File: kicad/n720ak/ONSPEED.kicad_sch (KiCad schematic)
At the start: 3 parts, among them J401 ONSPEED VOLUME POT, J402 ONSPEED BUTTON, J403 ONSPEED DB25

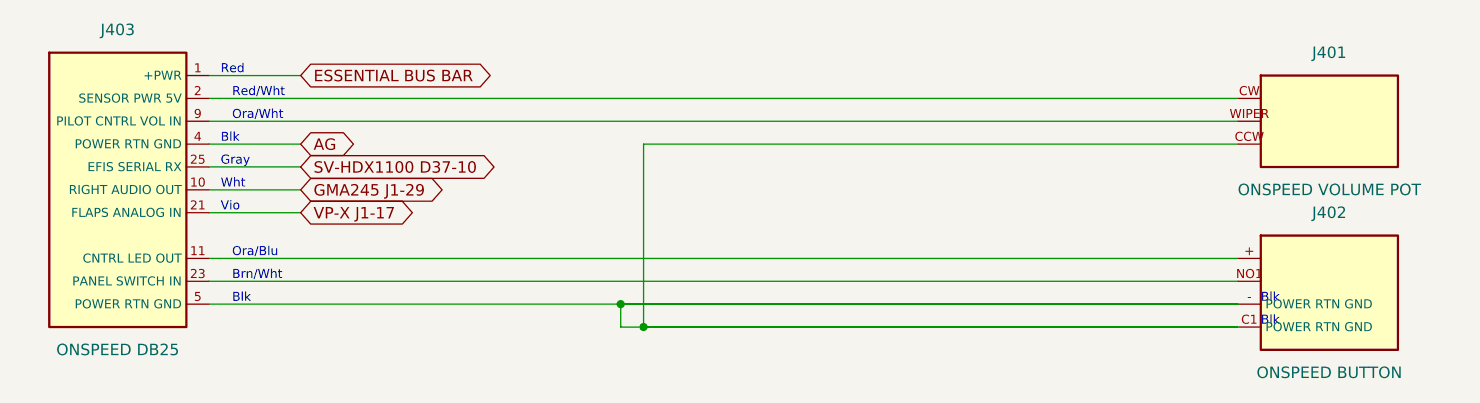
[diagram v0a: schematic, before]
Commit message: Record the third round of answers
- COM 2 flip/flop button returns to SV-COM-PANEL pin 3 (Ground out), on
  the owner's best recollection - recorded as unverified.
- OnSpeed's audio ground (pin 20) is tied to a ground pin in its own plug.
  GMA 245 Alert 3,4 Audio Lo (J1-43) is not connected, so the Alert 3
  input is single-ended.
- A panel switch disables the copilot grip trim by breaking the buttons'
  common. It is on neither SteinAir sheet, so it is recorded but flagged
  rather than drawn as a guess.
- AP disconnect is on both grips in parallel, as drawn.

Co-Authored-By: Claude Opus 5.5 <noreply@anthropic.com>
Claude-Session: https://claude.ai/code/session_015SpGdnvPFhutgEDurpngu2
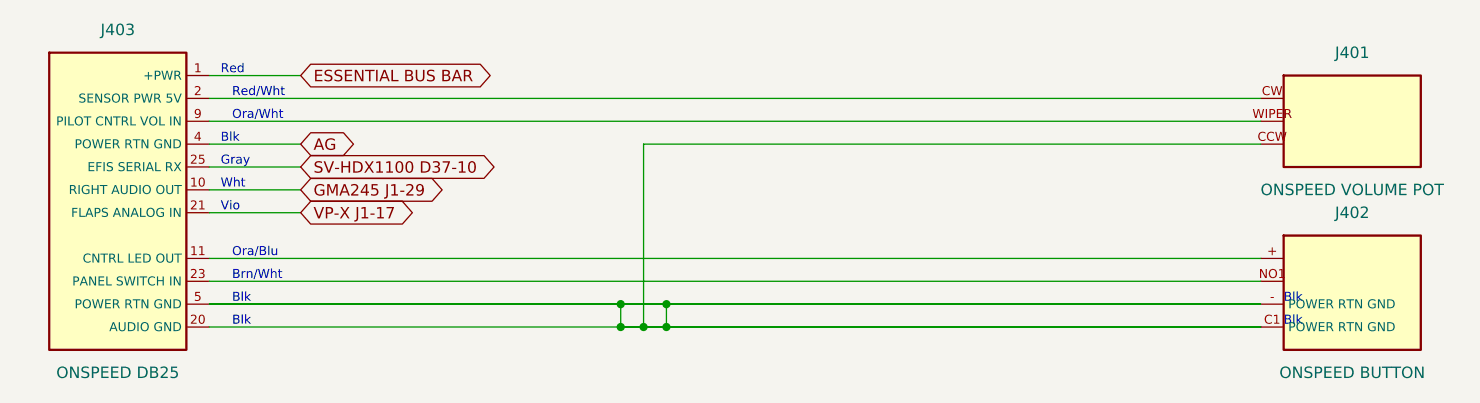
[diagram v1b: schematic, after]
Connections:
- net at J401.CCW, J402.- (POWER RTN GND), J402.C1 (POWER RTN GND)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: now also J403.20 (AUDIO GND)
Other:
- moved on the sheet: J401, J402
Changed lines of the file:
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@@
 	(paper "A3")
 	(title_block (title "OnSpeed AoA") (company "N720AK -- Van's RV-10") (comment 1 "Generated from wiring/ONSPEED.tsv -- edit the wire list, not this sheet"))
-	(symbol (lib_id "n720ak:ONSPEED_VOLUME_POT") (at 185.42 45.72 0) (unit 1)
+	(symbol (lib_id "n720ak:ONSPEED_VOLUME_POT") (at 187.96 45.72 0) (unit 1)
 		(in_bom yes) (on_board yes) (dnp no)
-		(property "Reference" "J401" (at 185.42 38.1 0) (effects (font (size 1.27 1.27))))
-		(property "Value" "ONSPEED VOLUME POT" (at 185.42 53.34 0) (effects (font (size 1.27 1.27))))
+		(property "Reference" "J401" (at 187.96 38.1 0) (effects (font (size 1.27 1.27))))
+		(property "Value" "ONSPEED VOLUME POT" (at 187.96 53.34 0) (effects (font (size 1.27 1.27))))
 		(instances (project "n720ak"
 			(path "/184b9d0a-f6b2-58e0-986b-f23064ec6643" (reference "J401") (unit 1))
 			(path "/05ae3897-9dd7-5bc2-b238-7f217081554a/2ac1f6a7-154c-57d3-8fed-8d80473941e2" (reference "J401") (unit 1)))))
-	(symbol (lib_id "n720ak:ONSPEED_BUTTON") (at 185.42 64.77 0) (unit 1)
+	(symbol (lib_id "n720ak:ONSPEED_BUTTON") (at 187.96 64.77 0) (unit 1)
 		(in_bom yes) (on_board yes) (dnp no)
-		(property "Reference" "J402" (at 185.42 55.88 0) (effects (font (size 1.27 1.27))))
-		(property "Value" "ONSPEED BUTTON" (at 185.42 73.66 0) (effects (font (size 1.27 1.27))))
+		(property "Reference" "J402" (at 187.96 55.88 0) (effects (font (size 1.27 1.27))))
+		(property "Value" "ONSPEED BUTTON" (at 187.96 73.66 0) (effects (font (size 1.27 1.27))))
 		(instances (project "n720ak"
 			(path "/184b9d0a-f6b2-58e0-986b-f23064ec6643" (reference "J402") (unit 1))
 			(path "/05ae3897-9dd7-5bc2-b238-7f217081554a/2ac1f6a7-154c-57d3-8fed-8d80473941e2" (reference "J402") (unit 1)))))
-	(symbol (lib_id "n720ak:ONSPEED_DB25") (at 50.8 53.34 0) (unit 1)
+	(symbol (lib_id "n720ak:ONSPEED_DB25") (at 50.8 54.61 0) (unit 1)
 		(in_bom yes) (on_board yes) (dnp no)
 		(property "Reference" "J403" (at 50.8 35.56 0) (effects (font (size 1.27 1.27))))
-		(property "Value" "ONSPEED DB25" (at 50.8 71.12 0) (effects (font (size 1.27 1.27))))
+		(property "Value" "ONSPEED DB25" (at 50.8 73.66 0) (effects (font (size 1.27 1.27))))
 		(instances (project "n720ak"
 			(path "/184b9d0a-f6b2-58e0-986b-f23064ec6643" (reference "J403") (unit 1))
@@
 	(wire (pts (xy 60.96 53.34) (xy 71.12 53.34)) (stroke (width 0) (type default)))
 	(wire (pts (xy 60.96 55.88) (xy 71.12 55.88)) (stroke (width 0) (type default)))
-	(wire (pts (xy 60.96 43.18) (xy 175.26 43.18)) (stroke (width 0) (type default)))
-	(wire (pts (xy 60.96 45.72) (xy 175.26 45.72)) (stroke (width 0) (type default)))
-	(wire (pts (xy 60.96 60.96) (xy 175.26 60.96)) (stroke (width 0) (type default)))
-	(wire (pts (xy 60.96 63.5) (xy 175.26 63.5)) (stroke (width 0) (type default)))
-	(wire (pts (xy 60.96 66.04) (xy 175.26 66.04)) (stroke (width 0) (type default)))
-	(wire (pts (xy 175.26 66.04) (xy 106.68 66.04)) (stroke (width 0) (type default)))
+	(wire (pts (xy 60.96 43.18) (xy 177.8 43.18)) (stroke (width 0) (type default)))
+	(wire (pts (xy 60.96 45.72) (xy 177.8 45.72)) (stroke (width 0) (type default)))
+	(wire (pts (xy 60.96 60.96) (xy 177.8 60.96)) (stroke (width 0) (type default)))
+	(wire (pts (xy 60.96 63.5) (xy 177.8 63.5)) (stroke (width 0) (type default)))
+	(wire (pts (xy 60.96 66.04) (xy 177.8 66.04)) (stroke (width 0) (type default)))
+	(wire (pts (xy 177.8 66.04) (xy 106.68 66.04)) (stroke (width 0) (type default)))
 	(wire (pts (xy 106.68 66.04) (xy 106.68 68.58)) (stroke (width 0) (type default)))
-	(wire (pts (xy 106.68 68.58) (xy 175.26 68.58)) (stroke (width 0) (type default)))
-	(wire (pts (xy 175.26 68.58) (xy 109.22 68.58)) (stroke (width 0) (type default)))
+	(wire (pts (xy 106.68 68.58) (xy 177.8 68.58)) (stroke (width 0) (type default)))
+	(wire (pts (xy 177.8 68.58) (xy 109.22 68.58)) (stroke (width 0) (type default)))
 	(wire (pts (xy 109.22 68.58) (xy 109.22 48.26)) (stroke (width 0) (type default)))
-	(wire (pts (xy 109.22 48.26) (xy 175.26 48.26)) (stroke (width 0) (type default)))
+	(wire (pts (xy 109.22 48.26) (xy 177.8 48.26)) (stroke (width 0) (type default)))
+	(wire (pts (xy 60.96 68.58) (xy 111.76 68.58)) (stroke (width 0) (type default)))
+	(wire (pts (xy 111.76 68.58) (xy 111.76 66.04)) (stroke (width 0) (type default)))
+	(wire (pts (xy 111.76 66.04) (xy 60.96 66.04)) (stroke (width 0) (type default)))
 	(junction (at 106.68 66.04) (diameter 0) (color 0 0 0 0))
+	(junction (at 106.68 68.58) (diameter 0) (color 0 0 0 0))
 	(junction (at 109.22 68.58) (diameter 0) (color 0 0 0 0))
+	(junction (at 111.76 66.04) (diameter 0) (color 0 0 0 0))
+	(junction (at 111.76 68.58) (diameter 0) (color 0 0 0 0))
 	(global_label "ESSENTIAL BUS BAR" (shape bidirectional) (at 71.12 40.64 0)
 		(effects (font (size 1.27 1.27)) (justify left)))
@@
 	(text "Brn/Wht" (at 63.5 63.5 0) (effects (font (size 1.0 1.0)) (justify left bottom)))
 	(text "Blk" (at 63.5 66.04 0) (effects (font (size 1.0 1.0)) (justify left bottom)))
-	(text "Blk" (at 177.8 66.04 0) (effects (font (size 1.0 1.0)) (justify left bottom)))
-	(text "Blk" (at 177.8 68.58 0) (effects (font (size 1.0 1.0)) (justify left bottom)))
+	(text "Blk" (at 180.34 66.04 0) (effects (font (size 1.0 1.0)) (justify left bottom)))
+	(text "Blk" (at 180.34 68.58 0) (effects (font (size 1.0 1.0)) (justify left bottom)))
+	(text "Blk" (at 63.5 68.58 0) (effects (font (size 1.0 1.0)) (justify left bottom)))
 	(sheet_instances (path "/" (page "1")))
 )
